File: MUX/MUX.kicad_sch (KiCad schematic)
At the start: 103 parts, among them P1 Conn_02x36_Top_Bottom, P2 DB9_Male, P3 DB9_Male, P4 DB9_Male, P5 DB9_Male

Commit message: Finished MUX
Merged in from Meisaka's repo
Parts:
- added R16: 1K, symbol Device:R
- U_B2: symbol 74xx:SN7425 -> 74xx_legacy:SN7425
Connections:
- net RTS4_TTL is gone; now on net RTS3_TTL: U_K8.7 (Q3), U_LL8.3
- net ~{ReadInput} is gone; now on net GND: U_B5.1 (OEa), U_B5.15 (OEb)
- net +5V: now also U_B2.14 (V_{CC}), R16.2; no longer U_B2.1 (V_{CC})
- net Data.InBD_{1}: now also U_H1.38 (CLS_{1}), U_H2.38 (CLS_{1}), U_H3.38 (CLS_{1})
- net GND: now also U_B2.7 (GND), U_C1.2 (Ia<b), U_C1.4 (Ia>b), U_C2.2 (Ia<b), U_C2.4 (Ia>b), U_C7.10 (CET), U_C7.9 (~{PE}); no longer U_B2.8 (GND)
- net RTS1_TTL: now also U_K8.5 (Q1), U_L8.3; no longer U_K8.4 (Q0), U_L8.2
- net RTS2_TTL: now also U_K8.6 (Q2), U_LL8.2; no longer U_K8.5 (Q1), U_L8.3
- net RTS3_TTL: no longer U_K8.6 (Q2), U_LL8.2
- net ~{Reset}: now also U_C8.13
- net TX_{2}_TTL: now reaches U_K6.10, U_L6.3
- net ~{TX_{2}_EIA}: now reaches P4.7, U_K6.11, U_K6.12
- net Write: now reaches U_B4.4, U_D2.12
- net Write: now also U_D1.2
- net INT_Pending: now reaches U_B7.9, U_E7.11
- net INT_Pending: now also U_B7.5
- net SysA_{2}: now reaches U_A1.6, U_B1.1, U_E2.13 (A2), U_E4.21 (A2)
- net CausePending: now reaches U_B1.11, U_B8.4 (~{S}), U_D8.6 (~{Q})
- net SysA_{3}: now reaches U_A1.12, U_B1.12, U_D1.3, U_D1.4, U_D1.5, U_E4.20 (A3)
- net SysA_{1}: now reaches U_A1.4, U_B1.2, U_B1.4, U_E2.14 (A1), U_E4.22 (A1)
- net SysA_{0}: now reaches U_A1.2, U_B1.3, U_E2.15 (A0), U_E4.23 (A0)
- net MMIO_HSel: now reaches U_B1.5, U_C1.3 (Ia=b), U_C2.6 (Oa=b)
- net CTS_{1}_TTL: now reaches U_F2.10 (I4), U_K6.2
- net LoadCR_{0}: now reaches U_E5.2, U_H1.34 (CRL), U_L1.13 (E01), U_L1.4 (E23)
- net ~{INT_Request}: now reaches U_A3.10, U_A7.10, U_B7.6, U_D8.2 (D)
- net INT_Request: now reaches U_A3.4, U_A7.5, U_A7.8, U_B7.1
- net ForceTXEInt: now reaches U_C6.10, U_C6.4, U_D3.8, U_E7.1, U_E7.4
- net ~{SysDataOutEN}: now reaches U_A5.9 (OE), U_A6.9 (OE), U_A8.8
- net TxBE_{3}: now reaches U_E3.11, U_E6.3 (C), U_F4.14 (I6)
- net RxD_{2}: now reaches U_F3.2 (I1), U_F5.6, U_F6.6 (D2)
- net ~{DirectRead}: now reaches U_C6.2, U_D1.8, U_E2.12 (A3)
- net at U_C6.3: now also U_A8.9; no longer U_D8.1 (~{R})
- net TX_{2}_OUT: now reaches U_H3.25 (TxOUT), U_K6.13
- net ~{RTS_{3}}: now reaches P5.4, U_LL8.6
- net ~{RTS_{2}}: now reaches P4.4, U_LL8.7
- net LoadCR_{1}: now reaches U_E5.4, U_H2.34 (CRL), U_L2.13 (E01), U_L2.4 (E23)
- net INR_OUT: now reaches U_A4.10, U_A4.13, U_A4.2, U_A4.4, U_A7.3
- net ~{ReadSR_{0}}: now reaches U_E1.13, U_E2.1 (0), U_F1.1 (OEa), U_F1.15 (OEb)
- net ~{ReadRxB_{0}}: now reaches U_E2.2 (1), U_H1.18 (~{RxDR}), U_H1.4 (~{RxB_OE})
- net ~{ReadSR_{1}}: now reaches U_E1.12, U_E2.3 (2), U_F2.1 (OEa), U_F2.15 (OEb)
- net ~{ReadRxB_{1}: now reaches U_E2.4 (3), U_H2.18 (~{RxDR}), U_H2.4 (~{RxB_OE})
- net ~{ReadSR_{2}}: now reaches U_E1.10, U_E2.5 (4), U_F3.1 (OEa), U_F3.15 (OEb)
- net ~{ReadRxB_{2}}: now reaches U_E2.6 (5), U_H3.18 (~{RxDR}), U_H3.4 (~{RxB_OE})
- net ~{ReadSR_{3}: now reaches U_E1.9, U_E2.7 (6), U_F4.1 (OEa), U_F4.15 (OEb)
- net ~{ReadRxB_{3}}: now reaches U_E2.9 (7), U_H4.18 (~{RxDR}), U_H4.4 (~{RxB_OE})
- net ~{INT_INH}: now reaches U_B7.10
- net ~{INT_INH}: now also U_A3.9, U_A8.12, U_B7.4
- net LevelAllow: now reaches U_B7.13
- net LevelAllow: now also U_A3.5, U_B3.7 (Oa<b)
- net ~{INTHandled}: now reaches U_C8.4, U_D8.5 (Q)
- net ~{INTHandled}: now also U_C8.1
- net RX_{3}_IN: now reaches U_H4.20 (RxIN), U_L7.10 (4Y)
- net RX_{2}_IN: now reaches U_H3.20 (RxIN), U_L7.12 (2Y)
- net ~{CTS_{2}}: now reaches P4.2, U_L7.4 (1A)
- net ~{RX_{2}}: now reaches P4.8, U_L7.5 (2A)
- net ~{CTS_{3}}: now reaches P5.2, U_L7.6 (3A)
- net ~{RX_{3}}: now reaches P5.8, U_L7.7 (4A)
- net CTS_{3}_TTL: now reaches U_F4.10 (I4), U_J6.2
- net FrameF_{3}: now reaches U_F4.12 (I5), U_H4.14 (FError)
- net RxD_{3}: now reaches U_F4.2 (I1), U_F5.8, U_F6.7 (D3)
- net ParityF_{3}: now reaches U_F4.4 (I2), U_H4.13 (PError)
- net OverrunF_{3}: now reaches U_F4.6 (I3), U_H4.15 (OError)
- net LoadCR_{2}: now reaches U_E5.6, U_H3.34 (CRL), U_L3.13 (E01), U_L3.4 (E23)
- net Read: now reaches U_B4.2, U_D2.11, U_D3.3
- net Read: now also U_D1.9
- net at U_D2.13: now also U_D2.2
- net TxBE_{1}: now reaches U_D6.11 (C), U_E3.6, U_F2.14 (I6)
- net TX_{1}_TTL: now reaches U_K6.4, U_LL6.3
- net ~{TX_{1}}: now reaches P3.6, U_LL6.6
- net TX_{3}_OUT: now reaches U_H4.25 (TxOUT), U_J5.13
- net LoadCR_{3}: now reaches U_E5.10, U_H4.34 (CRL), U_L4.13 (E01), U_L4.4 (E23)
- net ~{CauseHold}: now reaches U_E7.8, U_F6.13 (E01), U_F6.4 (E23), U_F7.13 (E01), U_F7.4 (E23)
- net TX_{3}_TTL: now reaches U_J5.4, U_L6.2
- net ~{TX_{2}}: now reaches P4.6, U_L6.6
- net ~{TX_{3}}: now reaches P5.6, U_L6.7
- net CTS_{2}_TTL: now reaches U_F3.10 (I4), U_J6.12
- net DirectAddressed: now reaches U_C1.6 (Oa=b), U_D1.1, U_D3.1
- net DirectAddressed: now also U_D1.11
- net ~{DirectAddressed}: now reaches U_D3.2
- net ~{DirectAddressed}: now also U_B6.1, U_D2.3
- net ParityF_{1}: now reaches U_F2.4 (I2), U_H2.13 (PError)
- net FrameF_{1}: now reaches U_H2.14 (FError)
- net FrameF_{1}: now also U_F2.12 (I5)
- net OverrunF_{1}: now reaches U_H2.15 (OError)
- net OverrunF_{1}: now also U_F2.6 (I3)
- net RX_{1}_IN: now reaches U_H2.20 (RxIN), U_L5.10 (4Y)
- net TX_{1}_OUT: now reaches U_H2.25 (TxOUT), U_J6.3
- net ~{CREndStrobe}: now reaches U_B8.5 (Q), U_C8.12
- net Phase3: now reaches U_C7.12 (Q2)
- net Phase3: now also U_D2.9
- net Phase2: now reaches U_C7.13 (Q1)
- net Phase2: now also U_C7.5 (D2)
- net Phase1: now reaches U_C7.14 (Q0), U_D1.13, U_J7.1
- net Phase1: now also U_C7.4 (D1)
- net at U_C7.3 (D0), U_C7.6 (D3): now also U_D8.1 (~{R}), R16.1
- net ~{TX_{3}_EIA}: now reaches P5.7, U_J5.12, U_J5.3
- net CommonRead: now reaches U_D2.4
- net CommonRead: now also U_D2.8, U_D3.5
- net ~{SelfReset}: now reaches U_A7.12, U_B6.13, U_B8.8 (~{Q})
- net ParityF_{2}: now reaches U_F3.4 (I2), U_H3.13 (PError)
- net FrameF_{2}: now reaches U_F3.12 (I5), U_H3.14 (FError)
- net OverrunF_{2}: now reaches U_F3.6 (I3), U_H3.15 (OError)
- net ~{CTS_{1}}: now reaches P3.2, U_L5.6 (3A)
- net ~{TX_{1}_EIA}: now reaches P3.7, U_J6.4, U_K6.3
- net ~{RX_{1}}: now reaches P3.8, U_L5.7 (4A)
- net CTS_{0}_TTL: now reaches U_F1.10 (I4), U_J5.10
- net FrameF_{0}: now reaches U_F1.12 (I5), U_H1.14 (FError)
- net TxBE_{0}: now reaches U_D6.3 (C), U_E3.3, U_F1.14 (I6)
- net ParityF_{0}: now reaches U_F1.4 (I2), U_H1.13 (PError)
- net OverrunF_{0}: now reaches U_F1.6 (I3), U_H1.15 (OError)
- net LoadIPL: now reaches U_C5.10 (CP), U_D3.12
- net ~{DirectWrite}: now reaches U_D1.12, U_E4.18 (E0), U_E4.19 (E1)
- net RX_{0}_IN: now reaches U_H1.20 (RxIN), U_L5.12 (2Y)
- net TxBE_{2}: now reaches U_E3.8, U_E6.11 (C), U_F3.14 (I6)
- net CTS1 renamed ~{CTS_{0}}
- net D4_1 renamed ~{CommonRead}
- net F6_D0 renamed RxD_{0}
- net F6_D1 renamed RxD_{1}
- net RTS1 renamed ~{RTS_{0}}
- net RTS2 renamed ~{RTS_{1}}
- net RTS_EN renamed ~{RTS_REG_EN}
- net RXD1 renamed ~{RX_{0}}
- net TXD1 renamed ~{TX_{0}}
- net TXD1_BUF renamed TX_{0}_TTL
- net TXD1_TTL renamed TX_{0}_OUT
- net ~{CBRL} renamed ~{LoadCBR}
- net ~{CRL1} renamed ~{LoadCR_{0}}
- net ~{CRL2} renamed ~{LoadCR_{1}}
- net ~{CRL3} renamed ~{LoadCR_{2}}
- net ~{CRL4} renamed ~{LoadCR_{3}}
- net ~{IPLL} renamed ~{LoadIPL}
- net ~{RTSL} renamed ~{LoadRTS}
- net ~{TXBL1} renamed ~{LoadTxB_{0}}
- net ~{TXBL2} renamed ~{LoadTxB_{1}}
- net ~{TXBL3} renamed ~{LoadTxB_{2}}
- net ~{TXBL4} renamed ~{LoadTxB_{3}}
- net ~{TXD1_TTL} renamed ~{TX_{0}_EIA}
- net ~{is_common_addressed} renamed ~{CommonAddressed}
- new net RTS0_TTL: U_K8.4 (Q0), U_L8.2
- no-connect marks 82 -> 136
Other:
- note added: "(-12V)"
- note added: "(GND)"
- note added: "(~{Reset})"
- note added: "(~{Set})"
- note added: "*^{1} Reading this register is only valid during an interrupt"
- note added: "*^{2} Baud = Crystal / (256 * (256 - N)); N != 0"
- note added: "1.5"
- note added: "1200"
- note added: "19200"
- note added: "2400"
- note added: "300"
- note added: "4"
- note added: "4800"
- note added: "4915200 MHz"
- note added: "5"
- note added: "6"
- note added: "7"
- note added: "75"
- note added: "8"
- note added: "9"
- note added: "9600"
- note added: "A"
- note added: "B"
- note added: "Baud"
- note added: "Baud Rate Gen Divide *^{2}"
- note added: "Baud Rate Select"
- note added: "C"
- note added: "CTS"
- note added: "Card Address"
- note added: "Card Number"
- note added: "Clear to Send (pin 2)"
- note added: "Control Bits"
- note added: "D"
- note added: "D8A when set, will always set B8A"
- note added: "Data"
- note added: "Data Bits Length"
- note added: "E"
- note added: "Even"
- note added: "F"
- note added: "F20F *^{1}"
- note added: "Force TXE MUX 3..0"
- note added: "FrEr"
- note added: "Framing Error"
- note added: "Interrupt Cause MMIO bits (0xF20F Read)"
- note added: "Interrupts Off (Any write)"
- note added: "Interrupts On (Any write)"
- note added: "Length Select"
- note added: "MUX 0"
- note added: "MUX 1"
- note added: "MUX 2"
- note added: "MUX 3"
- note added: "MUX Card Reset (Any write)"
- note added: "MUX0"
- note added: "N"
- note added: "N / 16"
- note added: "N / 2"
- note added: "N / 256"
- note added: "N / 4"
- note added: "N / 64"
- note added: "N / 8"
- note added: "N/A"
- note added: "OvRE"
- note added: "PDis"
- note added: "PEr"
- note added: "Parity 0=Enable, 1=Disable"
- note added: "Parity 0=Odd, 1=Even"
- note added: "Parity Mismatch Error"
- note added: "Q follows D when Enabled (H)"
- note added: "Rate Gen"
- note added: "Read"
- note added: "Receive Data Available"
- note added: "Receive Overrun"
- note added: "Reg"
- note added: "Rx Data"
- note added: "RxDi"
- note added: "Set IPL"
- note added: "Status Bits"
- note added: "Status registers only output 6 bits this drives the other 2 high bits to 0 (see U_D4)"
- note added: "Stop"
- note added: "Stop Bits Length"
- note added: "The shift function isn't even used. lul This register holds the value for the custom baud rate select. a 74LS273 might have been a better option"
- note added: "This counter pair provides a divide-by-N Loading the register will reset both counters this skews the output, so do not change while send or receive is in progress These count UP so the formula will be: Baud = MaxBaud / (256 - N) N must be less than 255 or it will not count *MaxBaud = Crystal / 256"
- note added: "Transmit Buffer Empty"
- note added: "Tx Data"
- note added: "TxEm"
- note added: "U_B2B matches the high nibble including ~{A_{15}} which on the CPU6, places the device in the 0x3Fnnn memory range for older buses, it's just 0xFnnn"
- note added: "Write"
- note added: "fanout is at most 12 did they assume that the 8835 can't drive that?"
- note added: "it's a shift register with reset! This provides the read/write cycle phases phase 1 is used to fetch data during write phase 3 will assert ~{DRDY} at cycle end"
- note added: "low register"
- note added: "this nand will go low when 0xF20F is accessed AND this device dispatched an interrupt"
- note removed: "(via)"
- note removed: "15 or 14? (needs lookup)"
- note removed: "A0"
- note removed: "A1"
- note removed: "A2"
- note removed: "A3"
- note removed: "C7(input) to D2.9 (via)"
- note removed: "D2.8/D3.5(via)"
- note removed: "E8"
- note removed: "E8 Func"
- note removed: "EN"
- note removed: "F8"
- note removed: "F8 Func"
- note removed: "I/O bits"
- note removed: "MUX4"
- note removed: "S0"
- note removed: "S1"
- note removed: "S2"
- note removed: "TODO"
- note removed: "The shift function isn't even used. lul"
- note removed: "This matches the high nibble including ~{A_{15}} which on the CPU6, places the device in the 0x3Fnnn memory range for older buses, it's just 0xFnnn"
- note removed: "addressed"
- note removed: "addressed (via)"
- note removed: "is read"
- note removed: "not high reg probably pin 10"
- note removed: "not write"
- note removed: "ok"
- note removed: "ok via"
- note removed: "read"
- note removed: "should connect data out? enable?"
- note removed: "should connect to buffer input"
- note removed: "this nand will go low when 0xF20F is accessed AND this device is interrupting AND interrupts are not preempted"
- note removed: "to reset?"
- note removed: "what even is this thing? is it right?"
- note removed: "write"
- note removed: "~{D5_En}"
- note removed: "~{is addressed}"
- note removed: "~{read}"
- moved on the sheet: JP1, JP2, JP3, JP4, P2, P3, P4, P5, R1, R10, R11, R12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

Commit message: MUX: Add packages
Set package info for all the parts
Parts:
- JP1, JP2, JP3, JP4: footprint (none) -> Connector_PinHeader_2.54mm:PinHeader_1x02_P2.54mm_Vertical
- P1: footprint (none) -> Connector_PCBEdge:BUS_EE200
- P2, P3, P4, P5: footprint (none) -> Connector_Dsub:DSUB-9_Male_Horizontal_P2.77x2.84mm_EdgePinOffset4.94mm_Housed_MountingHolesOffset7.48mm
- R1, R10, R11, R12, R13, R15, R16, R2, R20, R21, R3, R4, R5, R6, R7, R8, R9: footprint (none) -> Resistor_THT:R_Axial_DIN0204_L3.6mm_D1.6mm_P7.62mm_Horizontal
- SW_C3: footprint (none) -> Button_Switch_THT:SW_DIP_SPSTx04_Slide_6.7x11.72mm_W7.62mm_P2.54mm_LowProfile
- TP1: footprint (none) -> TestPoint:TestPoint_Plated_Hole_D2.0mm
- U_A1, U_A2, U_A3, U_A4, U_A7, U_A8, U_B1, U_B4, U_B6, U_B7, U_B8, U_C6, U_C8, U_D1, U_D2, U_D3, U_D6, U_D7, U_D8, U_E1, U_E3, U_E5, U_E6, U_E7, U_F5, U_J5, U_J6, U_J7, U_K6: footprint (none) -> Package_DIP:DIP-14_W7.62mm
- U_A5, U_A6, U_B3, U_B5, U_C1, U_C2, U_C5, U_C7, U_D4, U_D5, U_E2, U_E8, U_F1, U_F2, U_F3, U_F4, U_F6, U_F7, U_F8, U_H7, U_H8, U_K1, U_K2, U_K3, U_K4, U_K5, U_K7, U_K8, U_L1, U_L2, U_L3, U_L4, U_L5, U_L7: footprint (none) -> Package_DIP:DIP-16_W7.62mm
- U_E4, U_H6: footprint (none) -> Package_DIP:DIP-24_W15.24mm
- U_L6, U_L8, U_LL6, U_LL8: footprint (none) -> Package_DIP:DIP-8_W7.62mm
- XTAL1: footprint (none) -> Crystal:Crystal_HC18-U_Vertical

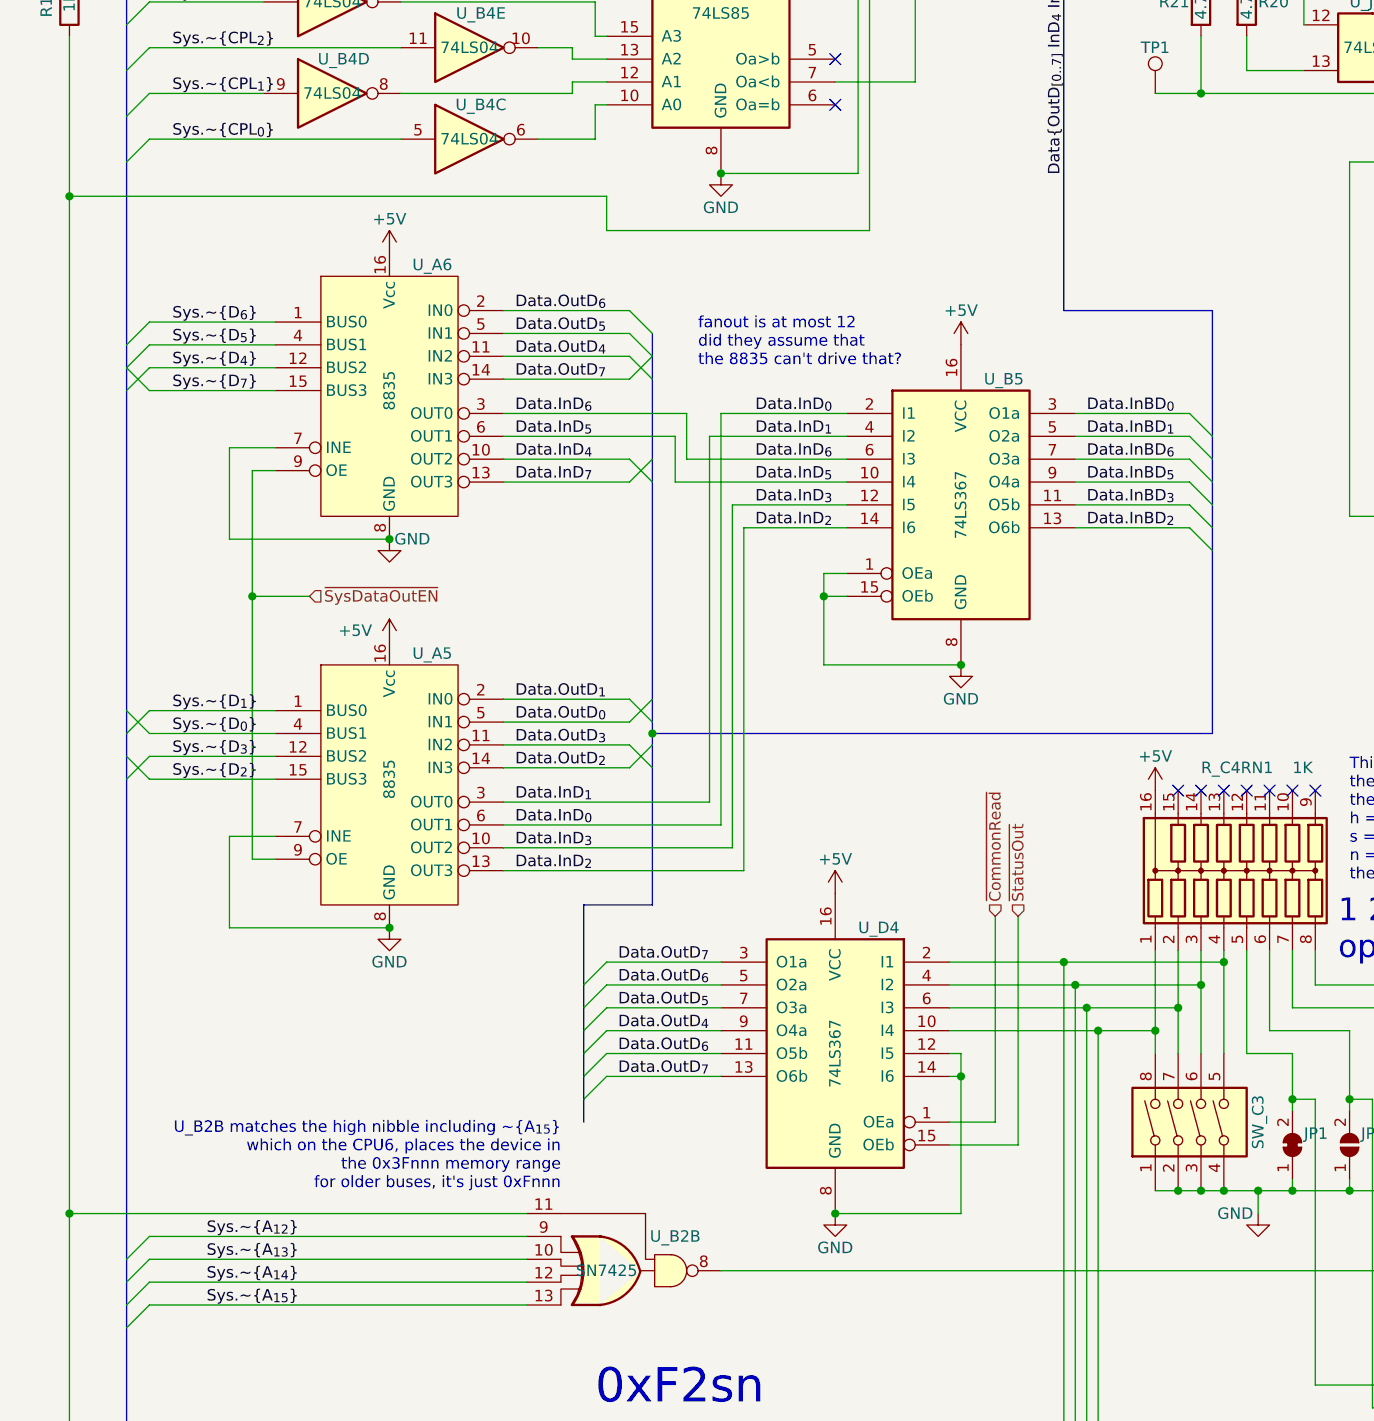
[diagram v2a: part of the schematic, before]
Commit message: Substitute 8835s
Substitute unobtanium chips with 74ls240's
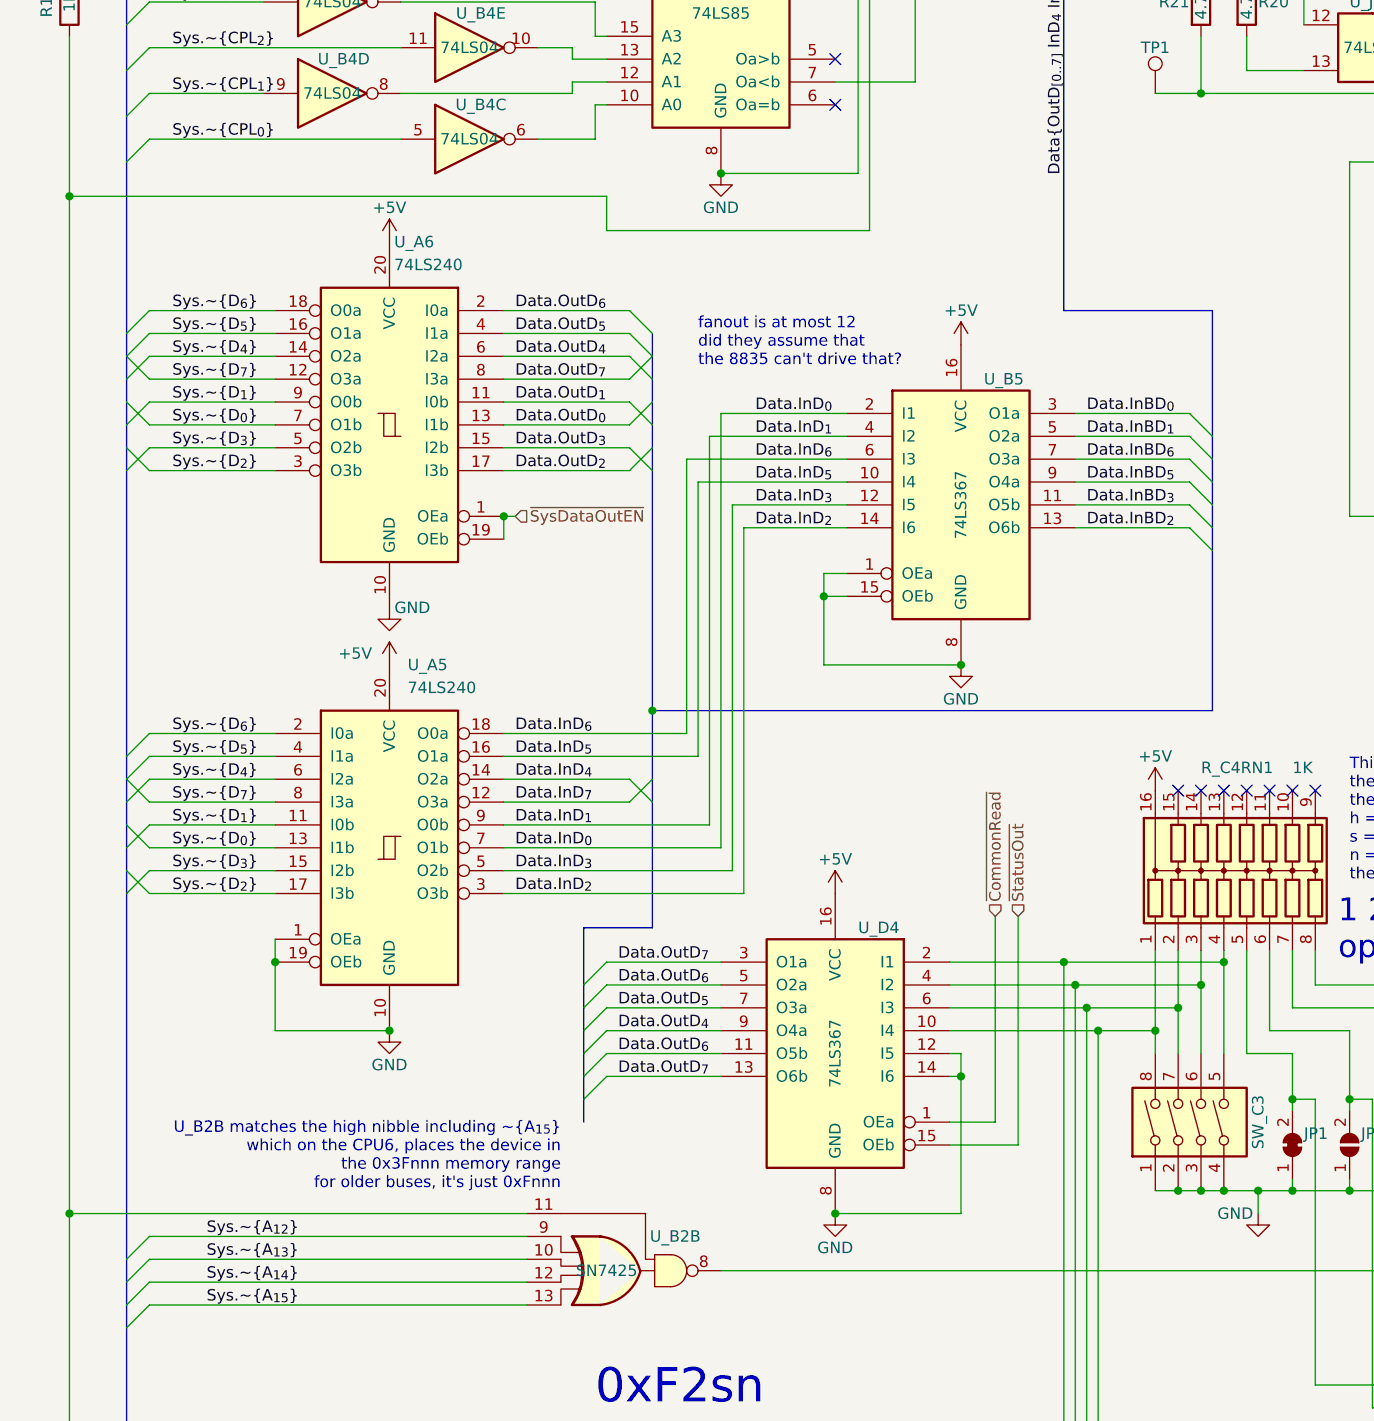
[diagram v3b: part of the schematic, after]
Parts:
- removed U_A5, U_A6: 8835, Package_DIP:DIP-16_W7.62mm, symbol Interface:8835
- added U_A5, U_A6: 74LS240, Package_DIP:DIP-20_W7.62mm, symbol 74xx:74LS240
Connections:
- net +5V: now also U_A5.20 (VCC), U_A6.20 (VCC)
- net Data.InD_{0}: now also U_A5.7 (O1b)
- net Data.InD_{1}: now also U_A5.9 (O0b)
- net Data.InD_{2}: now also U_A5.3 (O3b)
- net Data.InD_{3}: now also U_A5.5 (O2b)
- net Data.InD_{4}: now also U_A5.14 (O2a)
- net Data.InD_{5}: now also U_A5.16 (O1a)
- net Data.InD_{6}: now also U_A5.18 (O0a)
- net Data.InD_{7}: now also U_A5.12 (O3a)
- net Data.OutD_{0}: now also U_A6.13 (I1b)
- net Data.OutD_{1}: now also U_A6.11 (I0b)
- net Data.OutD_{2}: now also U_A6.17 (I3b)
- net Data.OutD_{3}: now also U_A6.15 (I2b)
- net Data.OutD_{4}: now also U_A6.6 (I2a)
- net Data.OutD_{5}: now also U_A6.4 (I1a)
- net Data.OutD_{6}: now also U_A6.2 (I0a)
- net Data.OutD_{7}: now also U_A6.8 (I3a)
- net GND: now also U_A5.1 (OEa), U_A5.10 (GND), U_A5.19 (OEb), U_A6.10 (GND)
- net Sys.~{D_{0}}: now also U_A5.13 (I1b), U_A6.7 (O1b)
- net Sys.~{D_{1}}: now also U_A5.11 (I0b), U_A6.9 (O0b)
- net Sys.~{D_{2}}: now also U_A5.17 (I3b), U_A6.3 (O3b)
- net Sys.~{D_{3}}: now also U_A5.15 (I2b), U_A6.5 (O2b)
- net Sys.~{D_{4}}: now also U_A5.6 (I2a), U_A6.14 (O2a)
- net Sys.~{D_{5}}: now also U_A5.4 (I1a), U_A6.16 (O1a)
- net Sys.~{D_{6}}: now also U_A5.2 (I0a), U_A6.18 (O0a)
- net Sys.~{D_{7}}: now also U_A5.8 (I3a), U_A6.12 (O3a)
- net ~{SysDataOutEN}: now also U_A6.1 (OEa), U_A6.19 (OEb)
